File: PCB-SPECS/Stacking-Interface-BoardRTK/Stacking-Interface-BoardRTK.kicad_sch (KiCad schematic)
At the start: 15 parts

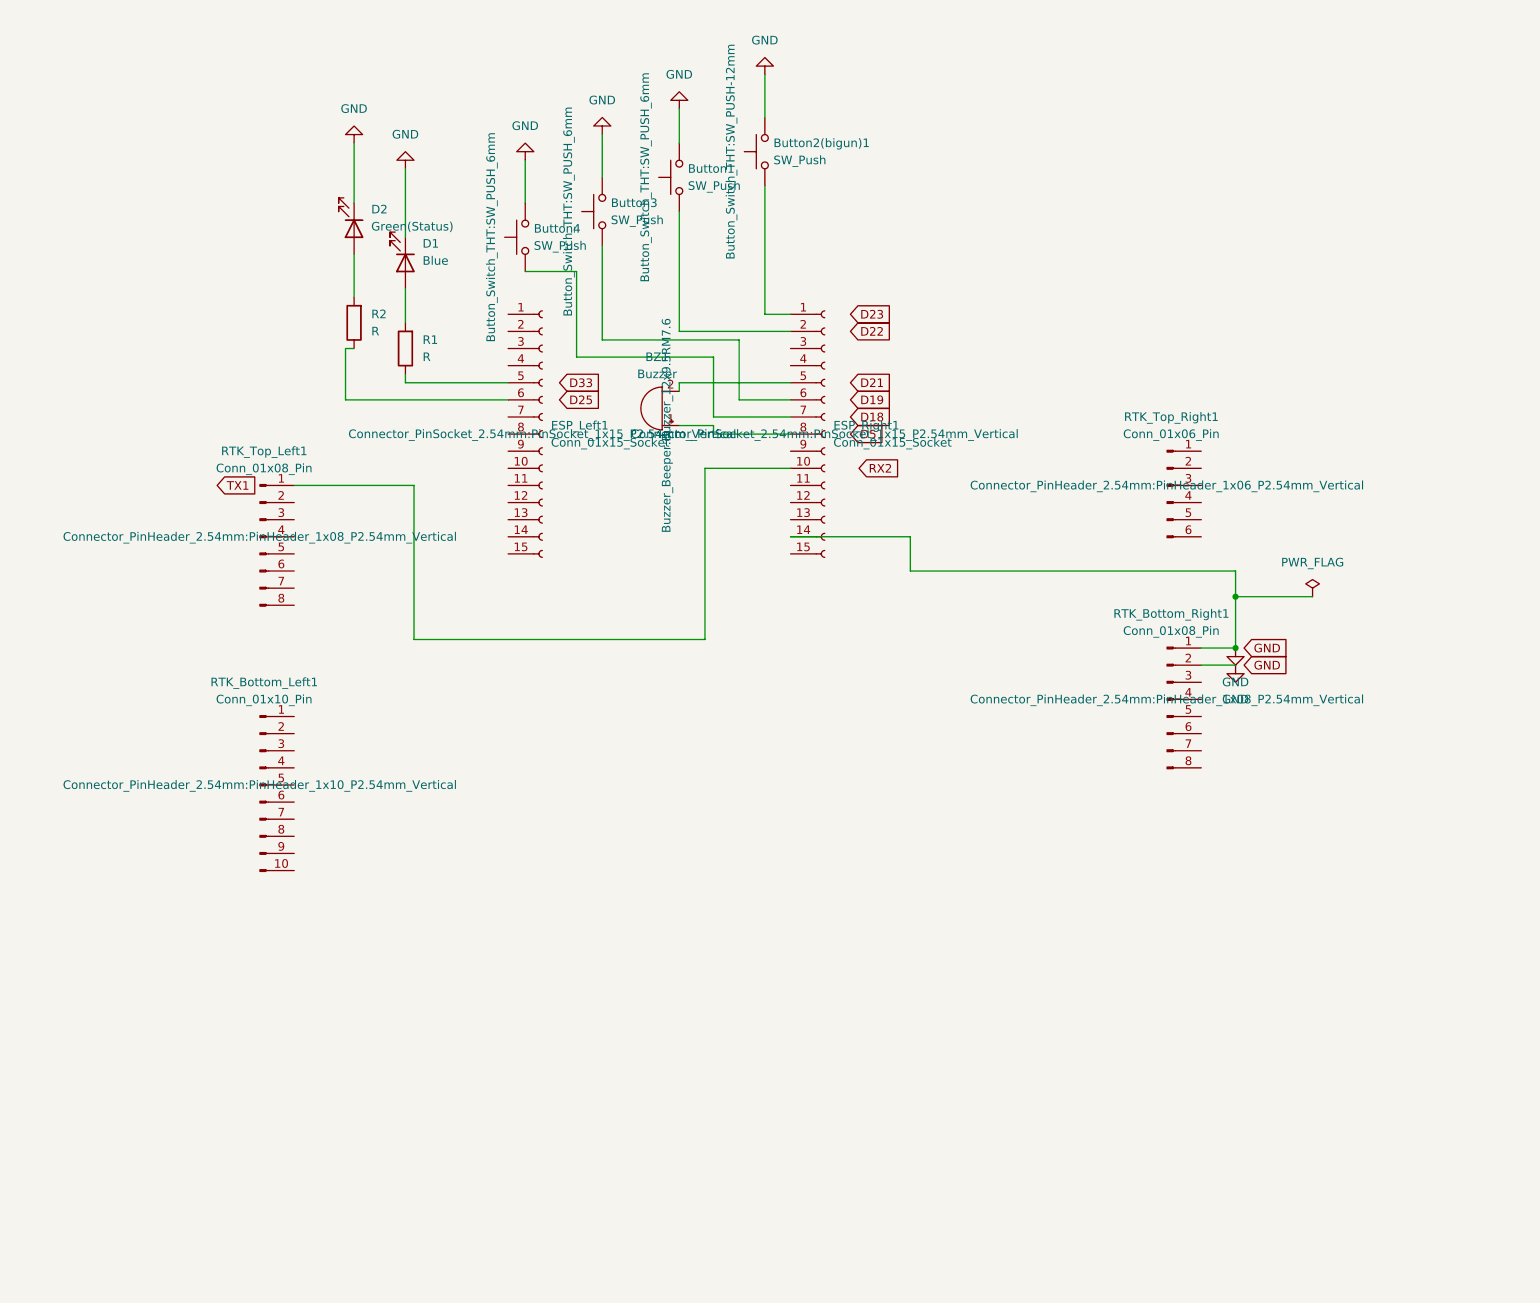
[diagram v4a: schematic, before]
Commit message: updating pcb
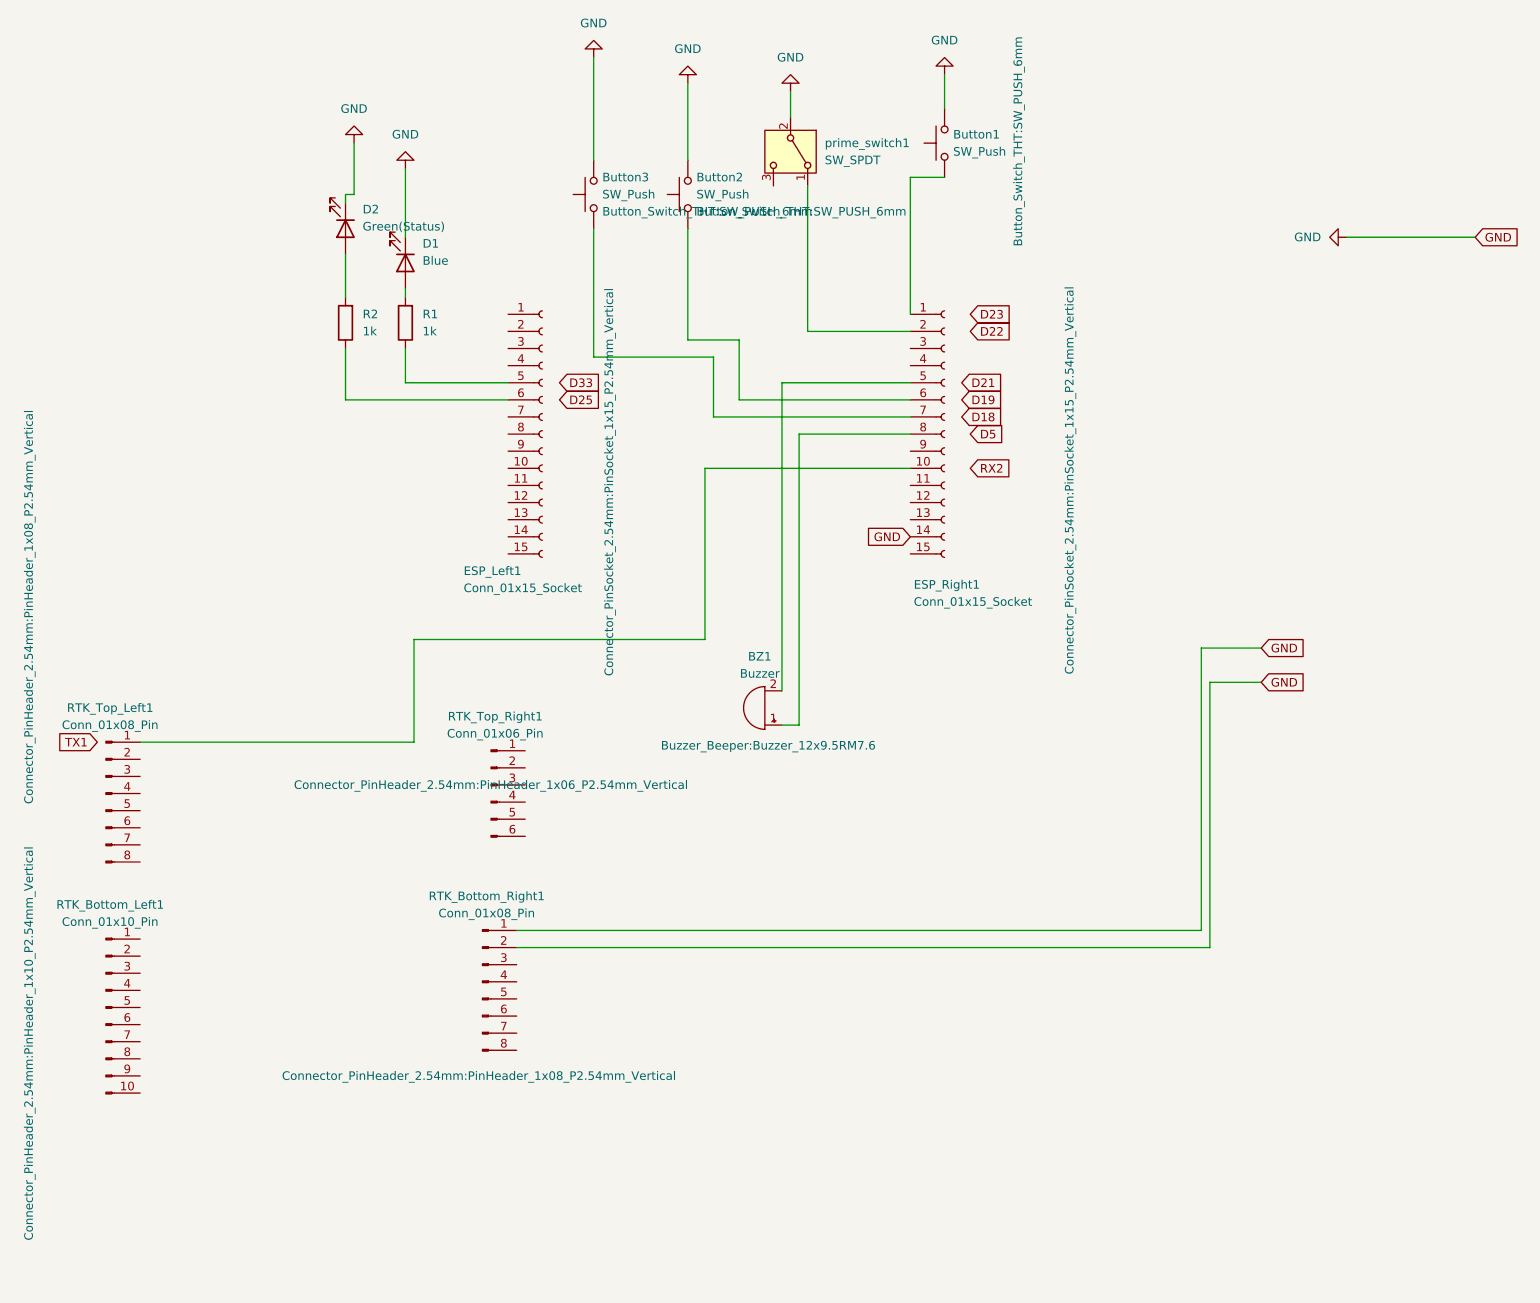
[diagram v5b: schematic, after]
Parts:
- removed Button2(bigun)1: SW_Push, Button_Switch_THT:SW_PUSH-12mm, symbol Switch:SW_Push
- added prime_switch1: SW_SPDT, Button_Switch_THT:SW_Slide-03_Wuerth-WS-SLTV_10x2.5x6.4_P2.54mm, symbol Switch:SW_SPDT
- D1, D2: footprint LED_SMD:LED_0603_1608Metric -> LED_THT:LED_D1.8mm_W1.8mm_H2.4mm_Horizontal_O1.27mm_Z1.6mm
- R1, R2: value R -> 1k
- renumbered Button3 to Button2, Button4 to Button3
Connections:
- net GND: now also prime_switch1.2 (B)
- net at ESP_Right1.1 (Pin_1): now also Button1.1
- net at ESP_Right1.2 (Pin_2): now also prime_switch1.1 (A); no longer Button1.1
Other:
- moved on the sheet: BZ1, Button2, Button3, D2, ESP_Right1, R1, R2, RTK_Bottom_Left1, RTK_Bottom_Right1, RTK_Top_Left1, RTK_Top_Right1

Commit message: pcb done
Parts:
- BZ1: footprint Buzzer_Beeper:Buzzer_12x9.5RM7.6 -> Buzzer_Beeper:Buzzer_D14mm_H7mm_P10mm
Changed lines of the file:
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@@
 			)
 		)
-		(property "Footprint" "Buzzer_Beeper:Buzzer_12x9.5RM7.6"
+		(property "Footprint" "Buzzer_Beeper:Buzzer_D14mm_H7mm_P10mm"
 			(at 146.558 121.158 0)
 			(effects

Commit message: finished designing pcb
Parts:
- removed Button3: SW_Push, Button_Switch_THT:SW_PUSH_6mm, symbol Switch:SW_Push
- added J1: Screw_Terminal_01x02, TerminalBlock:TerminalBlock_Altech_AK300-2_P5.00mm, symbol Connector:Screw_Terminal_01x02
- prime_switch1: footprint Button_Switch_THT:SW_Slide-03_Wuerth-WS-SLTV_10x2.5x6.4_P2.54mm -> watermelonstuff:spdt_switch
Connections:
- net GND: now also RTK_Bottom_Right1.3 (Pin_3), J1.1 (Pin_1); no longer RTK_Bottom_Right1.1 (Pin_1)
- net at ESP_Right1.7 (Pin_7): now also J1.2 (Pin_2)
- net VCC: now reaches ESP_Left1.15 (Pin_15)
- net VCC: now also RTK_Bottom_Right1.4 (Pin_4)
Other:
- note added: "D18"
- note added: "D19"
- note added: "D21"
- note added: "D22"
- note added: "D23"
- note added: "D25"
- note added: "D33"
- note added: "D5"
- note added: "RX2"
- note added: "TX1"
